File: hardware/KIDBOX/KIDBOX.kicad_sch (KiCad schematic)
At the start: 25 parts, among them J1 RP2350-Plus 1-20, J2 RP2350-Plus 21-40, J3 TFT ILI9341 2.4in, J4 TFT SD (apoyo), J5 DAC GY-PCM5102, SW1 DOWN, SW10 ON/OFF, SW2 LEFT, SW3 UP, SW4 RIGHT, SW5 SELECT, SW6 START, SW7 B, SW8 A, SW9 RESET

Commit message: Fase 1 v0.7: sin RESET frontal (SW9, C1), sin J4, SW10 con huella Wuerth 2.54 mm
- RUN (pin 30) queda no_connect; se elimina la red RUN.
- SW10: simbolo Switch:SW_SPDT_312 (comun = pin 1 = pad central de la huella
  SW_Slide-03_Wuerth-WS-SLTV_10x2.5x6.4_P2.54mm), pad 2 a GND, pad 3 sin conectar.
- J5: orden de pines confirmado, sin [SUPUESTO].
- ESPECIFICACION.md actualizada por el alumno (seccion 4 y 6).
- ERC 0 errores, BOM.csv y netlist.csv regenerados.

Co-Authored-By: Claude Opus 5.5 <noreply@anthropic.com>
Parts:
- removed C1: 100n, Capacitor_THT:C_Disc_D3.0mm_W1.6mm_P2.50mm, symbol Device:C
- removed J4: TFT SD (apoyo), Connector_PinSocket_2.54mm:PinSocket_1x04_P2.54mm_Vertical, symbol Connector_Generic:Conn_01x04
- removed SW9: RESET, Button_Switch_THT:SW_PUSH_6mm, symbol Switch:SW_Push
- SW10: footprint Button_Switch_THT:SW_Slide_SPDT_Straight_CK_OS102011MS2Q -> Button_Switch_THT:SW_Slide-03_Wuerth-WS-SLTV_10x2.5x6.4_P2.54mm; symbol Switch:SW_SPDT -> Switch:SW_SPDT_312
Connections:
- net GND: now also SW10.2 (C); no longer SW10.1 (A)
- net PWR_EN: now also SW10.1 (B); no longer SW10.2 (B)
- net RUN: no longer names the net of J2.10 (Pin_10)
- no-connect marks 23 -> 20
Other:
- note added: "Encendido (3V3_EN). Sin reset propio: RUN sin conectar (BOOT/RESET del módulo)"
- note added: "Generado con scripts/gen_esquematico.py desde scripts/kidbox_datos.py (ESPECIFICACION.md v0.7). No editar a mano: editar los datos y regenerar."
- note added: "H1–H4: M2, fijación a la carcasa · H5–H6: M3, agujeros del módulo de pantalla (lado de J3)"
- note added: "Orden de pines de J5 confirmado con la serigrafía de la pieza (14-oct)"
- note added: "SW10: común = pin 1 (pad central de la huella Würth) a 3V3_EN; OFF = pin 2 a GND; pin 3 al aire"
- note removed: "1 SD_CS"
- note removed: "2 SD_MOSI"
- note removed: "3 SD_MISO"
- note removed: "4 SD_CLK"
- note removed: "Generado con scripts/gen_esquematico.py desde scripts/kidbox_datos.py (ESPECIFICACION.md v0.6). No editar a mano: editar los datos y regenerar."
- note removed: "H1–H4: M2, fijación a la carcasa · H5–H6: M3, separadores de la pantalla (posición en Fase 2)"
- note removed: "J4: solo apoyo mecánico (lado SD), sin conectar"
- note removed: "Orden de pines de J5 [SUPUESTO: foto del vendedor] — confirmar con la pieza el 14-oct"
- note removed: "Reset (RUN) y encendido (3V3_EN)"
- note removed: "SW10: común (2) a 3V3_EN; OFF = pin 1 a GND; ON = pin 3 al aire"
- moved on the sheet: SW10

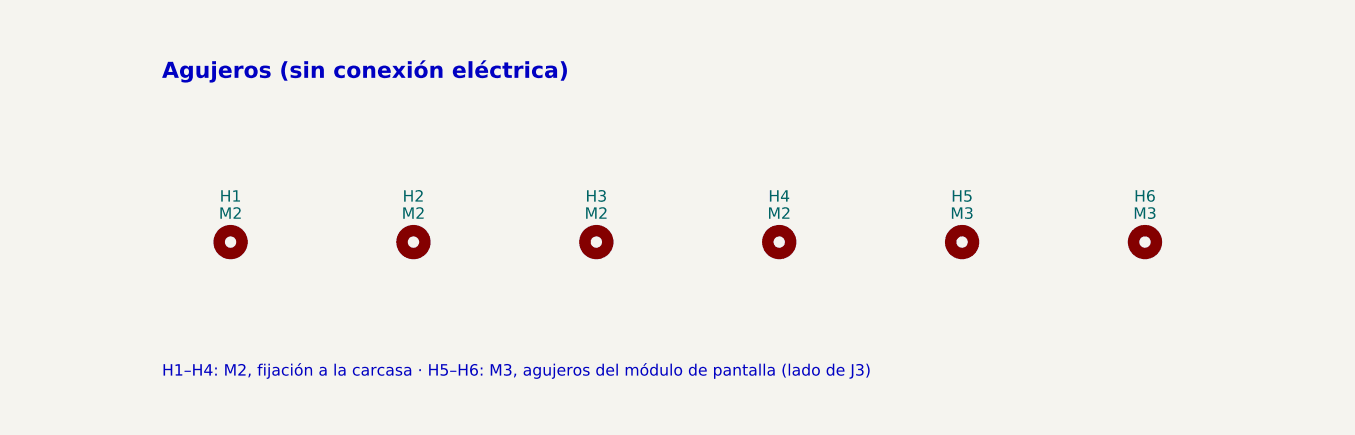
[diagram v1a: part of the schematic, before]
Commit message: Fase 2 PCB KIDBOX + correcciones de revision (sin H5/H6, SELECT/START a 66.5/83.5)
- scripts/gen_pcb.py: PCB completo generado con pcbnew (contorno 150x65 r4,
  H1-H4, huellas oficiales en las posiciones de la seccion 6, 0 vias, pistas
  en F.Cu, plano GND continuo en B.Cu con alivios termicos, serigrafia).
- J5 con VIN a la derecha visto de frente (I2S sin cruces ni vias); 3V3 a
  VIN por un puente pad a pad en B.Cu; PWR_EN por el borde superior.
- Revision del alumno: se eliminan H5/H6 y la regla de KIDBOX.kicad_dru;
  SW5/SW6 a x = 66.5 / 83.5 para sacar el cobre de START de la zona de bateria.
- verificar.py: ERC 0, DRC 0 errores / 0 avisos, 0 sin conectar, paridad 0.

Co-Authored-By: Claude Opus 5.5 <noreply@anthropic.com>
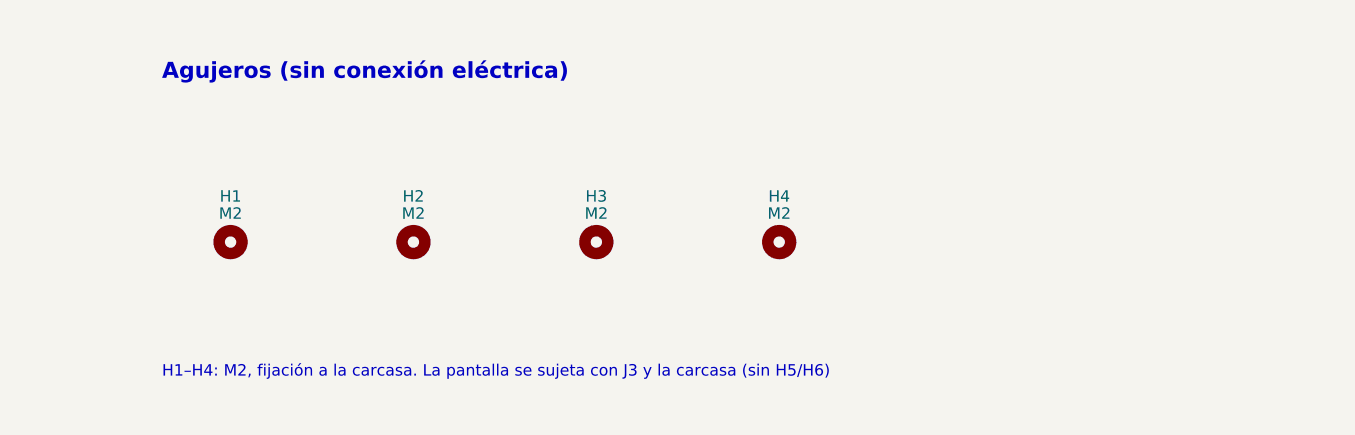
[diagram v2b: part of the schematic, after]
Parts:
- removed H5, H6: M3, MountingHole:MountingHole_3.2mm_M3, symbol Mechanical:MountingHole
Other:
- note added: "H1–H4: M2, fijación a la carcasa. La pantalla se sujeta con J3 y la carcasa (sin H5/H6)"
- note removed: "H1–H4: M2, fijación a la carcasa · H5–H6: M3, agujeros del módulo de pantalla (lado de J3)"
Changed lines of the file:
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@@
 		)
 	)
-	(symbol
-		(lib_id "Mechanical:MountingHole")
-		(at 271.78 220.98 0)
-		(unit 1)
-		(body_style 1)
-		(exclude_from_sim no)
-		(in_bom no)
-		(on_board yes)
-		(in_pos_files yes)
-		(dnp no)
-		(property "Reference" "H5"
-				(at 271.78 215.9 0)
-				(show_name no)
-				(do_not_autoplace no)
-				(effects
-					(font
-						(size 1.27 1.27)
-					)
-				)
-			)
-		(property "Value" "M3"
-				(at 271.78 217.805 0)
-				(show_name no)
-				(do_not_autoplace no)
-				(effects
-					(font
-						(size 1.27 1.27)
-					)
-				)
-			)
-		(property "Footprint" "MountingHole:MountingHole_3.2mm_M3"
-				(at 271.78 220.98 0)
-				(show_name no)
-				(do_not_autoplace no)
-				(hide yes)
-				(effects
-					(font
-						(size 1.27 1.27)
-					)
-				)
-			)
-		(property "Datasheet" ""
-				(at 271.78 220.98 0)
-				(show_name no)
-				(do_not_autoplace no)
-				(hide yes)
-				(effects
-					(font
-						(size 1.27 1.27)
-					)
-				)
-			)
-		(property "Description" "Mounting Hole without connection"
-				(at 271.78 220.98 0)
-				(show_name no)
-				(do_not_autoplace no)
-				(hide yes)
-				(effects
-					(font
-						(size 1.27 1.27)
-					)
-				)
-			)
-		(instances
-			(project "KIDBOX"
-				(path "/991b7356-9e94-5b24-b2e1-ea42da63d907"
-					(reference "H5")
-					(unit 1)
-				)
-			)
-		)
-	)
-	(symbol
-		(lib_id "Mechanical:MountingHole")
-		(at 292.1 220.98 0)
-		(unit 1)
-		(body_style 1)
-		(exclude_from_sim no)
-		(in_bom no)
-		(on_board yes)
-		(in_pos_files yes)
-		(dnp no)
-		(property "Reference" "H6"
-				(at 292.1 215.9 0)
-				(show_name no)
-				(do_not_autoplace no)
-				(effects
-					(font
-						(size 1.27 1.27)
-					)
-				)
-			)
-		(property "Value" "M3"
-				(at 292.1 217.805 0)
-				(show_name no)
-				(do_not_autoplace no)
-				(effects
-					(font
-						(size 1.27 1.27)
-					)
-				)
-			)
-		(property "Footprint" "MountingHole:MountingHole_3.2mm_M3"
-				(at 292.1 220.98 0)
-				(show_name no)
-				(do_not_autoplace no)
-				(hide yes)
-				(effects
-					(font
-						(size 1.27 1.27)
-					)
-				)
-			)
-		(property "Datasheet" ""
-				(at 292.1 220.98 0)
-				(show_name no)
-				(do_not_autoplace no)
-				(hide yes)
-				(effects
-					(font
-						(size 1.27 1.27)
-					)
-				)
-			)
-		(property "Description" "Mounting Hole without connection"
-				(at 292.1 220.98 0)
-				(show_name no)
-				(do_not_autoplace no)
-				(hide yes)
-				(effects
-					(font
-						(size 1.27 1.27)
-					)
-				)
-			)
-		(instances
-			(project "KIDBOX"
-				(path "/991b7356-9e94-5b24-b2e1-ea42da63d907"
-					(reference "H6")
-					(unit 1)
-				)
-			)
-		)
-	)
-	(text "H1–H4: M2, fijación a la carcasa · H5–H6: M3, agujeros del módulo de pantalla (lado de J3)"
+	(text "H1–H4: M2, fijación a la carcasa. La pantalla se sujeta con J3 y la carcasa (sin H5/H6)"
 		(exclude_from_sim no)
 		(at 182.88 236.22 0)

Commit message: Fase 4: fabricacion PRELIMINAR
Paquete para JLCPCB (2 capas) en fabricacion/: Gerbers, taladros Excellon
(PTH/NPTH separados, origen absoluto, mapas PDF), KIDBOX_gerbers_PRELIMINAR.zip
y PDF 1:1 de frente y reverso; README.md con el aviso PRELIMINAR - NO FABRICAR,
orden de soldadura, parametros de pedido y revision en el visor.

Incluye las correcciones de la Fase 3 (rondas 2 y 3): DAC horizontal (J5 en
x = 59, C3/C4, I2S y 3V3 re-ruteados, sin pistas en B.Cu), min_connection 0.2,
C4 10u 25V, huellas con hoja/filtros/unidades (F8 sin cambios), OFF/ON en SW10,
KIDBOX/.history/ en .gitignore, verificar_extra.py y la especificacion
actualizada por el alumno. El .kicad_pcb no cambio en la Fase 4.

Co-Authored-By: Claude Opus 5.5 <noreply@anthropic.com>
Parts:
- C4: value 10u 16V -> 10u 25V
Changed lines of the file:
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@@
 				)
 			)
-		(property "Value" "10u 16V"
+		(property "Value" "10u 25V"
 				(at 366.395 83.82 0)
 				(show_name no)
@@
 		(in_bom no)
 		(on_board yes)
-		(in_pos_files yes)
+		(in_pos_files no)
 		(dnp no)
 		(property "Reference" "H1"
@@
 		(in_bom no)
 		(on_board yes)
-		(in_pos_files yes)
+		(in_pos_files no)
 		(dnp no)
 		(property "Reference" "H2"
@@
 		(in_bom no)
 		(on_board yes)
-		(in_pos_files yes)
+		(in_pos_files no)
 		(dnp no)
 		(property "Reference" "H3"
@@
 		(in_bom no)
 		(on_board yes)
-		(in_pos_files yes)
+		(in_pos_files no)
 		(dnp no)
 		(property "Reference" "H4"

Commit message: v0.8: C2 y C3 con huella de paso 5 mm
Co-Authored-By: Claude Opus 5.5 <noreply@anthropic.com>
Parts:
- C2, C3: footprint Capacitor_THT:C_Disc_D3.0mm_W1.6mm_P2.50mm -> Capacitor_THT:C_Disc_D5.0mm_W2.5mm_P5.00mm
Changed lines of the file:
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@@
 				)
 			)
-		(property "Footprint" "Capacitor_THT:C_Disc_D3.0mm_W1.6mm_P2.50mm"
+		(property "Footprint" "Capacitor_THT:C_Disc_D5.0mm_W2.5mm_P5.00mm"
 				(at 265.1252 85.09 0)
 				(show_name no)
@@
 				)
 			)
-		(property "Footprint" "Capacitor_THT:C_Disc_D3.0mm_W1.6mm_P2.50mm"
+		(property "Footprint" "Capacitor_THT:C_Disc_D5.0mm_W2.5mm_P5.00mm"
 				(at 351.4852 85.09 0)
 				(show_name no)

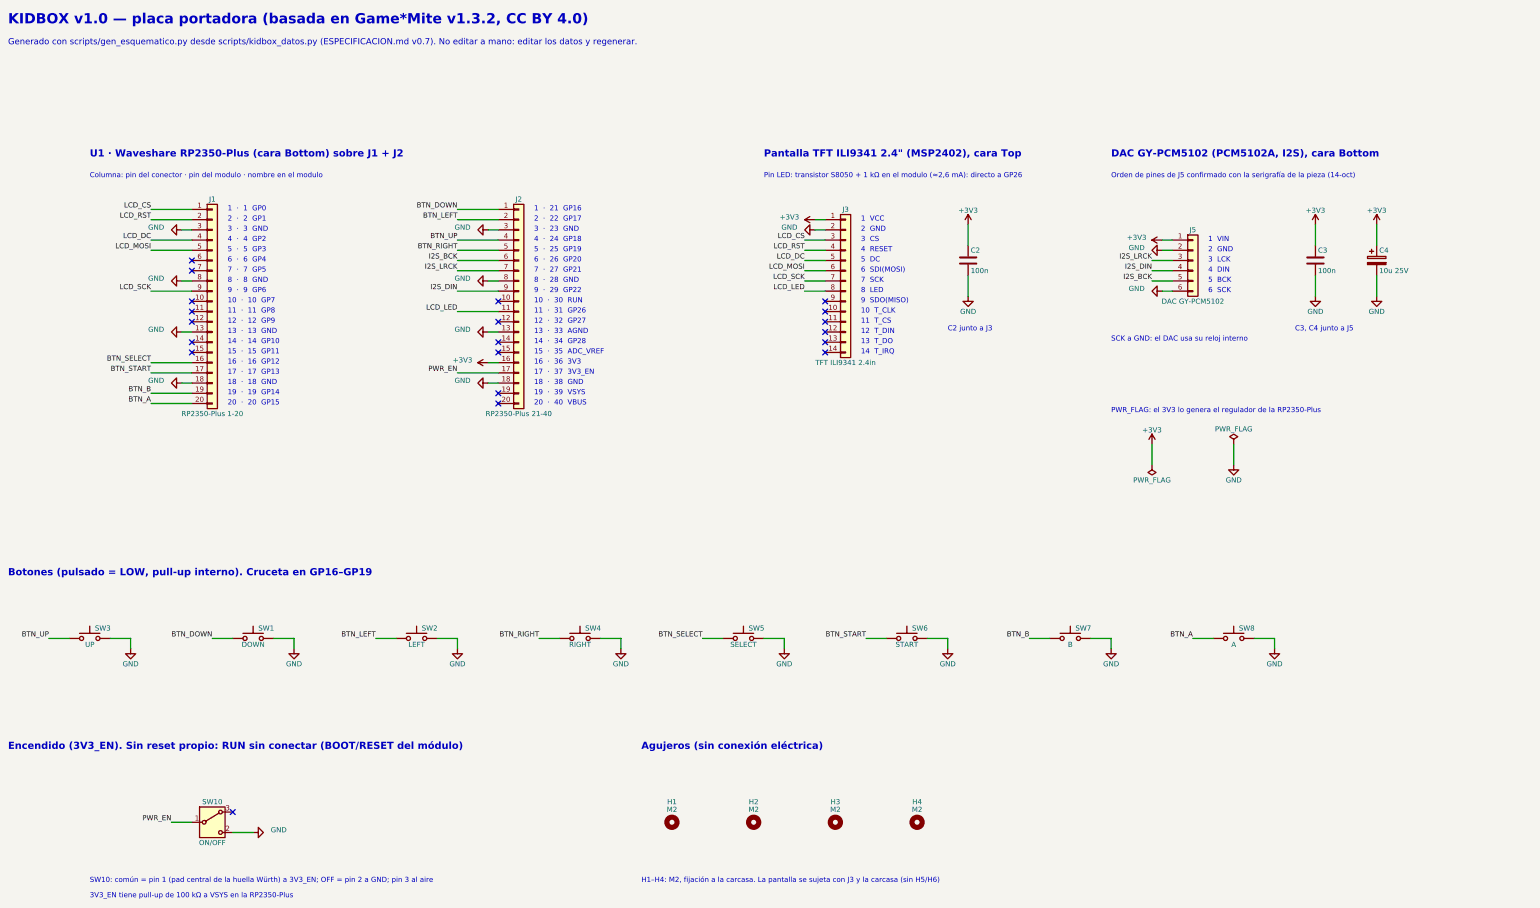
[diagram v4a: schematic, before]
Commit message: v0.9: 155x75, simetría, imagen centrada, DAC adelante, correcciones del profesor
- Placa 155 x 75 (r = 4), agujeros M2 en (4,4), (151,4), (4,71), (151,71); eje de simetría x = 77.5.
- Imagen de la pantalla centrada (módulo en x = 73.5, J3 en x = 36.91); RP2350-Plus centrado (68.61 / 86.39);
  zona de batería x 90.5-126.0.
- DAC adelante con huella propia Connector_KIDBOX:GY-PCM5102_1x06_P2.54mm (KIDBOX/KIDBOX.pretty, gen_huella_dac.py):
  jack centrado en x = 77.5 con la boca en y = 75; C3 y C4 junto a VIN, fuera del DAC.
- Controles simétricos: cruceta (18, 44), A/B (142, 39)/(132, 49), SELECT/START (41, 67)/(114, 67); SW10 atrás en (50, 8).
- Correcciones del profesor: 3V3 sin pasar entre pines de J3 (0.25 mm en J2), LRCK fuera de J5 (cruza J2.30/J2.29),
  BCK a 0.85 mm de J2.21, reglas .kicad_dru de 0.29 mm, C4 en CP_Radial_D4.0mm_P1.50mm, TP1/TP2, BT1 excluida de la
  placa, PWR_EN lejos del borde, rótulos 1.2/0.18, v0.9 en serigrafía, cajetín, README y zip.
- BOM de compra completa (BOM_compra.csv), PDF 1:1 en A4 y Carta, carpeta de entrega (gen_entrega.py).
- ESPECIFICACION.md v0.9, DECISIONES.md sección 16, README reescrito.

verificar.py: SIN ERRORES (ERC 0/0, DRC 0/0, sin conectar 0, paridad 0).
verificar_extra.py: 0 con los tests ignorados activados; F8 en seco 0 cambios.

Co-Authored-By: Claude Opus 5.5 <noreply@anthropic.com>
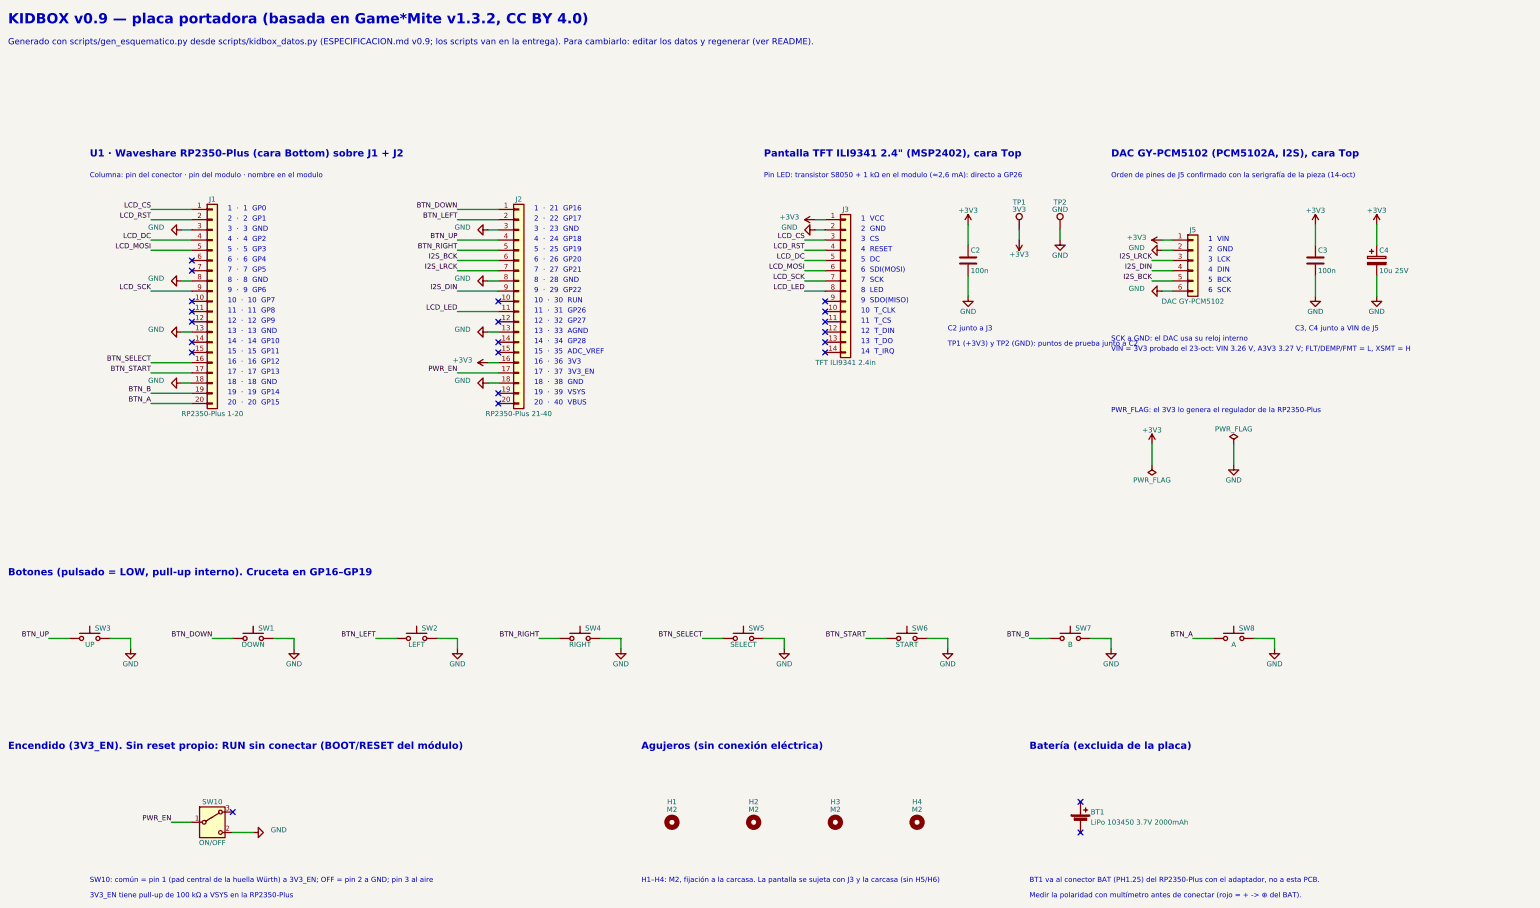
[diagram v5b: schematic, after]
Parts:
- added BT1: LiPo 103450 3.7V 2000mAh, symbol Device:Battery_Cell
- added TP1: 3V3, TestPoint:TestPoint_THTPad_D2.0mm_Drill1.0mm, symbol Connector:TestPoint
- added TP2: GND, TestPoint:TestPoint_THTPad_D2.0mm_Drill1.0mm, symbol Connector:TestPoint
- C4: footprint Capacitor_THT:CP_Radial_D5.0mm_P2.00mm -> Capacitor_THT:CP_Radial_D4.0mm_P1.50mm
- J5: footprint Connector_PinSocket_2.54mm:PinSocket_1x06_P2.54mm_Vertical -> Connector_KIDBOX:GY-PCM5102_1x06_P2.54mm
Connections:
- net +3V3: now also TP1.1
- net GND: now also TP2.1
- no-connect marks 20 -> 22
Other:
- note added: "BT1 va al conector BAT (PH1.25) del RP2350-Plus con el adaptador, no a esta PCB."
- note added: "Batería (excluida de la placa)"
- note added: "C3, C4 junto a VIN de J5"
- note added: "DAC GY-PCM5102 (PCM5102A, I2S), cara Top"
- note added: "Generado con scripts/gen_esquematico.py desde scripts/kidbox_datos.py (ESPECIFICACION.md v0.9; los scripts van en la entrega). Para cambiarlo: editar los datos y regenerar (ver README)."
- note added: "KIDBOX v0.9 — placa portadora (basada en Game*Mite v1.3.2, CC BY 4.0)"
- note added: "Medir la polaridad con multímetro antes de conectar (rojo = + -> ⊕ del BAT)."
- note added: "TP1 (+3V3) y TP2 (GND): puntos de prueba junto a C2"
- note added: "VIN = 3V3 probado el 23-oct: VIN 3.26 V, A3V3 3.27 V; FLT/DEMP/FMT = L, XSMT = H"
- note removed: "C3, C4 junto a J5"
- note removed: "DAC GY-PCM5102 (PCM5102A, I2S), cara Bottom"
- note removed: "Generado con scripts/gen_esquematico.py desde scripts/kidbox_datos.py (ESPECIFICACION.md v0.7). No editar a mano: editar los datos y regenerar."
- note removed: "KIDBOX v1.0 — placa portadora (basada en Game*Mite v1.3.2, CC BY 4.0)"

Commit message: v1.0: pistas a 45°, prueba 1:1, versión de fabricación
Revisión 2 del profesor:
- gen_pcb.py reemplaza cada codo a 90° por un chaflán a 45° (d = 1.0 mm, o largo/2; menor si hace falta para
  0.29 mm a pads y 0.30 mm a pistas). Esquinas a 90°: 33 -> 0 (112 a 45°, 3 colineales). Sin mover huellas.
- verificar_extra.py cuenta las esquinas de pista y falla si queda alguna a 90°.
- Prueba 1:1 de la 150 x 70 (27-oct): fotos en KIDBOX/verificacion/, pendiente cerrado; BOM_compra con un
  100 nF más de repuesto (C2 perdido); README: batería con el cable hacia el conector BAT.
- Versión de fabricación v1.0: serigrafía, cajetín, ESPECIFICACION, README (sin PRELIMINAR), zip
  KIDBOX_gerbers_v1.0.zip y carpeta de entrega. DECISIONES.md sección 18.

verificar.py: SIN ERRORES (ERC 0/0, DRC 0/0, sin conectar 0, paridad 0).
verificar_extra.py: 0 con los tests ignorados activados; F8 en seco 0 cambios; 0 esquinas a 90°.

Co-Authored-By: Claude Opus 5.5 <noreply@anthropic.com>
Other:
- note added: "Generado con scripts/gen_esquematico.py desde scripts/kidbox_datos.py (ESPECIFICACION.md v1.0; los scripts van en la entrega). Para cambiarlo: editar los datos y regenerar (ver README)."
- note added: "KIDBOX v1.0 — placa portadora (basada en Game*Mite v1.3.2, CC BY 4.0)"
- note removed: "Generado con scripts/gen_esquematico.py desde scripts/kidbox_datos.py (ESPECIFICACION.md v0.9; los scripts van en la entrega). Para cambiarlo: editar los datos y regenerar (ver README)."
- note removed: "KIDBOX v0.9 — placa portadora (basada en Game*Mite v1.3.2, CC BY 4.0)"
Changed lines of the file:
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@@
 	(title_block
 		(title "KIDBOX")
-		(date "2026-10-26")
-		(rev "v0.9")
+		(date "2026-10-27")
+		(rev "v1.0")
 		(company "Equipo KIDBOX")
 		(comment 1 "Basado en Game*Mite v1.3.2 de Thomas Hugo Williams (CC BY 4.0)")
-		(comment 2 "ESPECIFICACION.md v0.9")
+		(comment 2 "ESPECIFICACION.md v1.0")
 	)
-	(text "KIDBOX v0.9 — placa portadora (basada en Game*Mite v1.3.2, CC BY 4.0)"
+	(text "KIDBOX v1.0 — placa portadora (basada en Game*Mite v1.3.2, CC BY 4.0)"
 		(exclude_from_sim no)
 		(at 25.4 22.86 0)
@@
 		)
 	)
-	(text "Generado con scripts/gen_esquematico.py desde scripts/kidbox_datos.py (ESPECIFICACION.md v0.9; los scripts van en la entrega). Para cambiarlo: editar los datos y regenerar (ver README)."
+	(text "Generado con scripts/gen_esquematico.py desde scripts/kidbox_datos.py (ESPECIFICACION.md v1.0; los scripts van en la entrega). Para cambiarlo: editar los datos y regenerar (ver README)."
 		(exclude_from_sim no)
 		(at 25.4 27.94 0)
